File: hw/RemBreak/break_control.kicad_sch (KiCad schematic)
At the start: 13 parts, among them J6 Conn_01x07, J7 Conn_01x07, J8 Conn_01x03, Q10 BC337, Q11 BC847

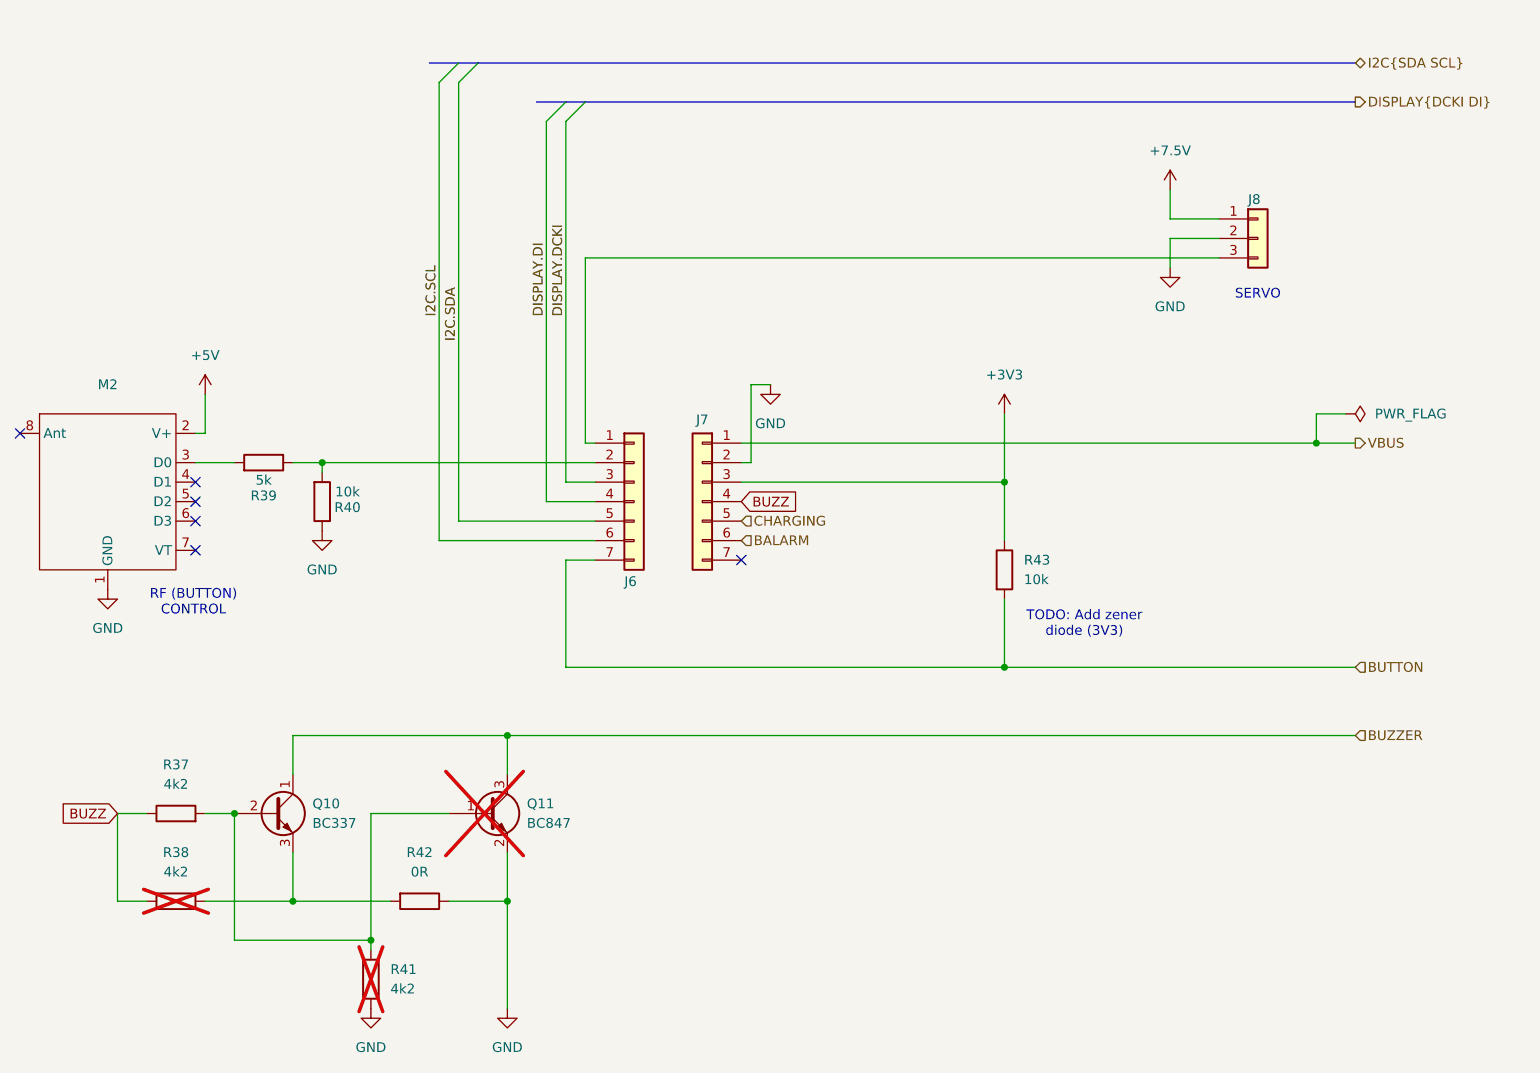
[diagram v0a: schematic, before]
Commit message: first version of routing finished
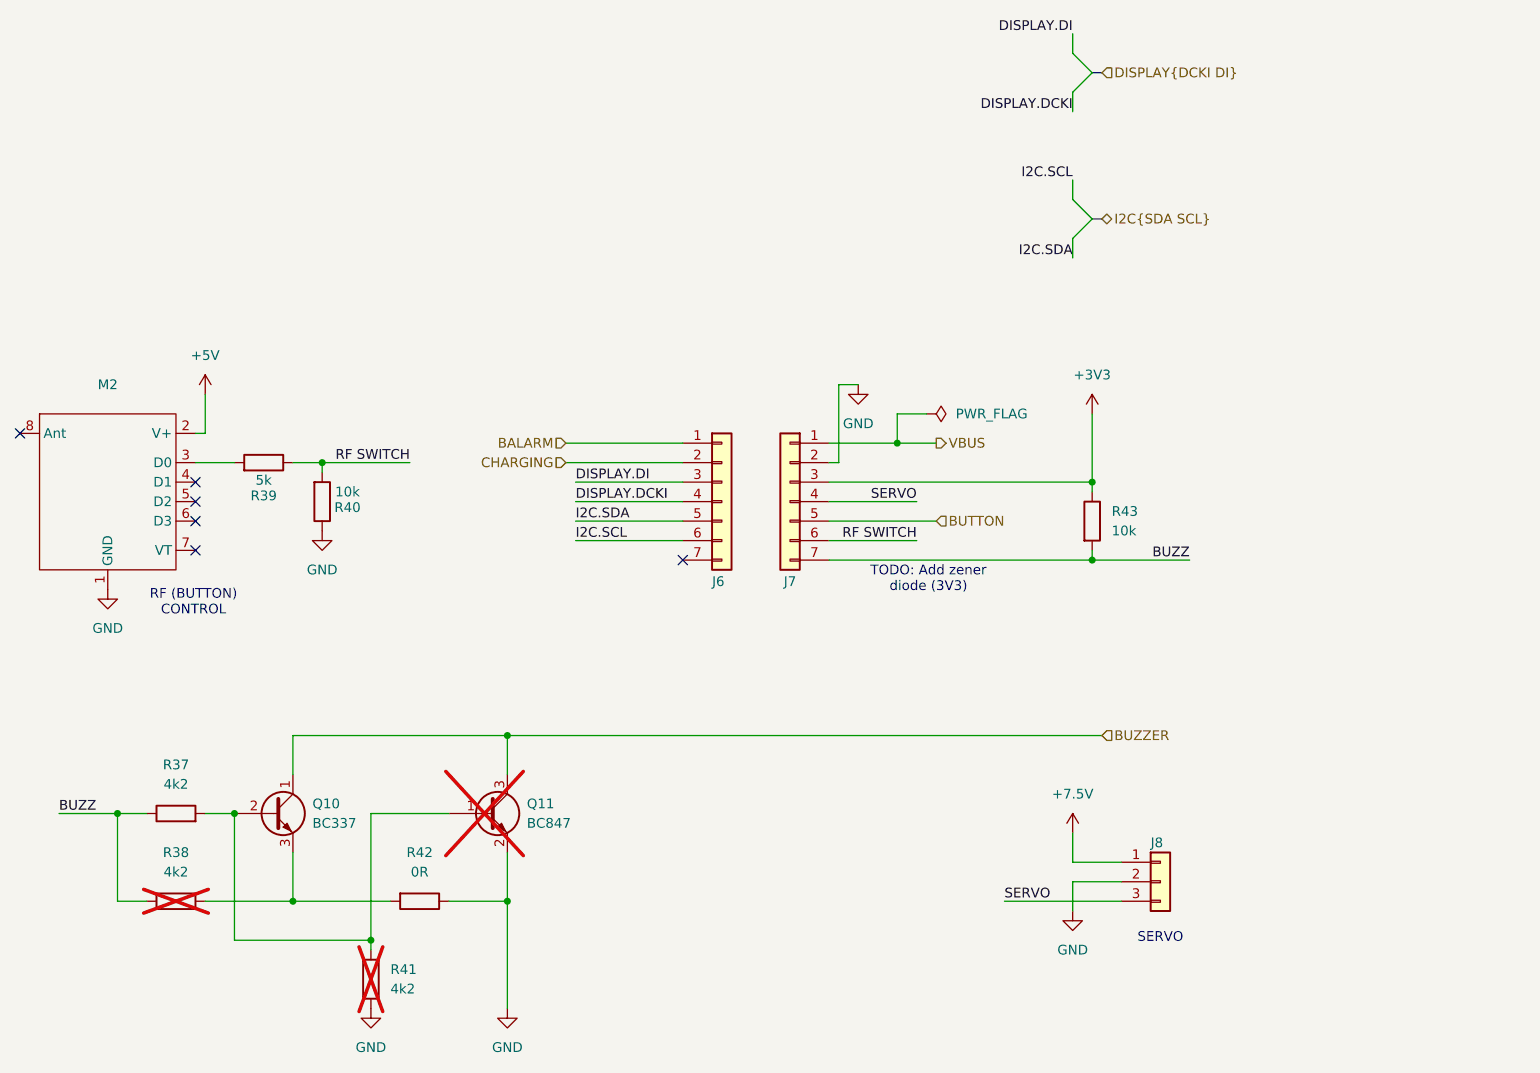
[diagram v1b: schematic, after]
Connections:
- net BALARM: now also J6.1 (Pin_1); no longer J7.6 (Pin_6)
- net BUTTON: now also J7.5 (Pin_5); no longer J6.7 (Pin_7), R43.2
- net BUZZ: now also J7.7 (Pin_7), R43.2; no longer J7.4 (Pin_4)
- net CHARGING: now also J6.2 (Pin_2); no longer J7.5 (Pin_5)
- net DISPLAY.DCKI: now also J6.4 (Pin_4); no longer J6.3 (Pin_3)
- net DISPLAY.DI: now also J6.3 (Pin_3); no longer J6.4 (Pin_4)
- net SERVO: now reaches J8.3 (Pin_3)
- net SERVO: now also J7.4 (Pin_4); no longer J6.1 (Pin_1)
- net RF SWITCH: now reaches R39.1, R40.2
- net RF SWITCH: now also J7.6 (Pin_6); no longer J6.2 (Pin_2)
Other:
- moved on the sheet: J6, J7, J8, R43

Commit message: changed board settings and replaced r and c footprints with the ones for handsoldering
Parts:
- R37, R38, R39, R40, R41, R42, R43: footprint Resistor_SMD:R_0805_2012Metric -> Resistor_SMD:R_0805_2012Metric_Pad1.20x1.40mm_HandSolder
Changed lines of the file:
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@@
 			)
 		)
-		(property "Footprint" "Resistor_SMD:R_0805_2012Metric"
+		(property "Footprint" "Resistor_SMD:R_0805_2012Metric_Pad1.20x1.40mm_HandSolder"
 			(at 74.93 136.398 90)
 			(effects
@@
 			)
 		)
-		(property "Footprint" "Resistor_SMD:R_0805_2012Metric"
+		(property "Footprint" "Resistor_SMD:R_0805_2012Metric_Pad1.20x1.40mm_HandSolder"
 			(at 192.532 96.52 90)
 			(effects
@@
 			)
 		)
-		(property "Footprint" "Resistor_SMD:R_0805_2012Metric"
+		(property "Footprint" "Resistor_SMD:R_0805_2012Metric_Pad1.20x1.40mm_HandSolder"
 			(at 106.68 144.272 90)
 			(effects
@@
 			)
 		)
-		(property "Footprint" "Resistor_SMD:R_0805_2012Metric"
+		(property "Footprint" "Resistor_SMD:R_0805_2012Metric_Pad1.20x1.40mm_HandSolder"
 			(at 74.93 147.828 90)
 			(effects
@@
 			)
 		)
-		(property "Footprint" "Resistor_SMD:R_0805_2012Metric"
+		(property "Footprint" "Resistor_SMD:R_0805_2012Metric_Pad1.20x1.40mm_HandSolder"
 			(at 102.108 156.21 90)
 			(effects
@@
 			)
 		)
-		(property "Footprint" "Resistor_SMD:R_0805_2012Metric"
+		(property "Footprint" "Resistor_SMD:R_0805_2012Metric_Pad1.20x1.40mm_HandSolder"
 			(at 86.36 90.678 90)
 			(effects
@@
 			)
 		)
-		(property "Footprint" "Resistor_SMD:R_0805_2012Metric"
+		(property "Footprint" "Resistor_SMD:R_0805_2012Metric_Pad1.20x1.40mm_HandSolder"
 			(at 92.202 93.98 90)
 			(effects

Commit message: components placed and tracks routed - missing gnd connections and have to refactor the resistors under MCU
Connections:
- net BUTTON: now also J7.6 (Pin_6); no longer J7.5 (Pin_5)
- net CHARGING: now also J7.5 (Pin_5); no longer J6.2 (Pin_2)
- net RF SWITCH: now also J6.2 (Pin_2); no longer J7.6 (Pin_6)
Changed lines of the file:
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@@
+	(wire
+		(pts
+			(xy 127 88.9) (xy 140.97 88.9)
+		)
+		(stroke
+			(width 0)
+			(type default)
+		)
+	)
 	(wire
 		(pts
@@
 	(wire
 		(pts
-			(xy 160.02 99.06) (xy 171.45 99.06)
-		)
-		(stroke
-			(width 0)
-			(type default)
-		)
-	)
-	(wire
-		(pts
-			(xy 125.73 88.9) (xy 140.97 88.9)
+			(xy 160.02 99.06) (xy 173.99 99.06)
 		)
 		(stroke
@@
 	)
 	(label "RF SWITCH"
-		(at 171.45 99.06 180)
-		(fields_autoplaced yes)
-		(effects
-			(font
-				(size 1.27 1.27)
-			)
-			(justify right bottom)
+		(at 127 88.9 0)
+		(fields_autoplaced yes)
+		(effects
+			(font
+				(size 1.27 1.27)
+			)
+			(justify left bottom)
 		)
 	)
@@
 	(hierarchical_label "BUTTON"
 		(shape input)
-		(at 173.99 96.52 0)
+		(at 173.99 99.06 0)
 		(fields_autoplaced yes)
 		(effects
@@
 	(hierarchical_label "CHARGING"
 		(shape input)
-		(at 125.73 88.9 180)
-		(fields_autoplaced yes)
-		(effects
-			(font
-				(size 1.27 1.27)
-			)
-			(justify right)
-		)
-	)
+		(at 173.99 96.52 0)
+		(fields_autoplaced yes)
+		(effects
+			(font
+				(size 1.27 1.27)
+			)
+			(justify left)
+		)
+	)

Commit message: adjusting layout
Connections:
- net BALARM: now also J6.2 (Pin_2); no longer J6.1 (Pin_1)
- net RF SWITCH: now also J6.1 (Pin_1); no longer J6.2 (Pin_2)
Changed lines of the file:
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@@
 	(wire
 		(pts
-			(xy 125.73 86.36) (xy 140.97 86.36)
+			(xy 125.73 88.9) (xy 140.97 88.9)
 		)
 		(stroke
@@
 	(wire
 		(pts
-			(xy 127 88.9) (xy 140.97 88.9)
+			(xy 127 86.36) (xy 140.97 86.36)
 		)
 		(stroke
@@
 	)
 	(label "RF SWITCH"
-		(at 127 88.9 0)
+		(at 127 86.36 0)
 		(fields_autoplaced yes)
 		(effects
@@
 	(hierarchical_label "BALARM"
 		(shape input)
-		(at 125.73 86.36 180)
-		(fields_autoplaced yes)
-		(effects
+		(at 125.73 88.9 180)
+		(fields_autoplaced yes)
+		(effects

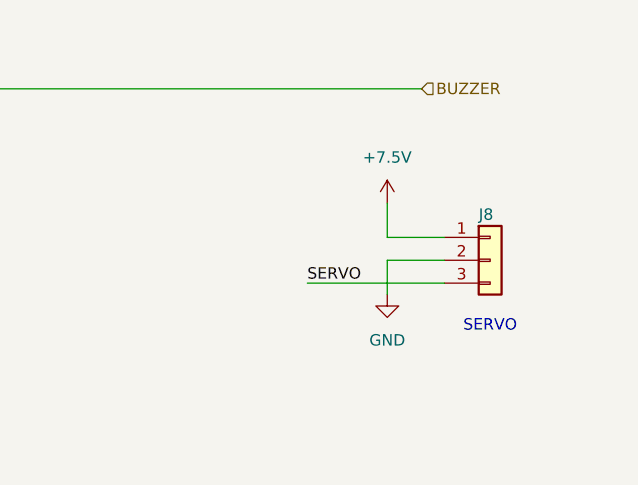
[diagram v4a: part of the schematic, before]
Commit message: middle part rerouted to fix the gnd connection
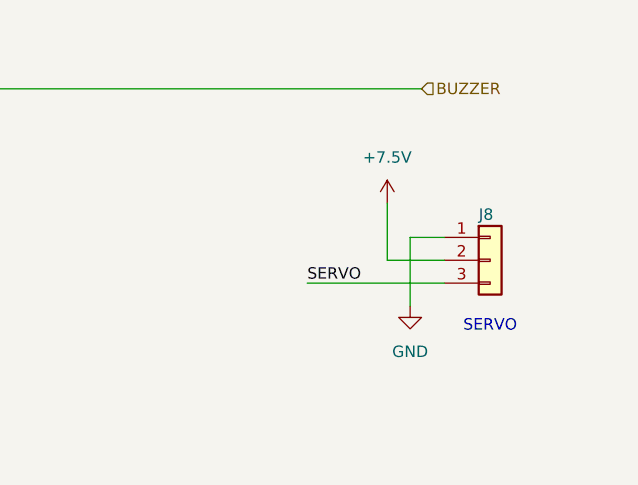
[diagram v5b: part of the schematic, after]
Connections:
- net +7.5V: now also J8.2 (Pin_2); no longer J8.1 (Pin_1)
- net GND: now also J8.1 (Pin_1); no longer J8.2 (Pin_2)
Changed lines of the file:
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@@
+	(wire
+		(pts
+			(xy 191.77 137.16) (xy 191.77 143.51)
+		)
+		(stroke
+			(width 0)
+			(type default)
+		)
+	)
 	(wire
 		(pts
@@
 	(wire
 		(pts
+			(xy 194.31 148.59) (xy 194.31 140.97)
+		)
+		(stroke
+			(width 0)
+			(type default)
+		)
+	)
+	(wire
+		(pts
 			(xy 182.88 146.05) (xy 198.12 146.05)
 		)
@@
 	(wire
 		(pts
+			(xy 191.77 143.51) (xy 198.12 143.51)
+		)
+		(stroke
+			(width 0)
+			(type default)
+		)
+	)
+	(wire
+		(pts
 			(xy 160.02 99.06) (xy 173.99 99.06)
 		)
@@
 	(wire
 		(pts
-			(xy 191.77 143.51) (xy 191.77 147.32)
-		)
-		(stroke
-			(width 0)
-			(type default)
-		)
-	)
-	(wire
-		(pts
 			(xy 100.33 134.62) (xy 110.49 134.62)
 		)
@@
 	(wire
 		(pts
-			(xy 191.77 140.97) (xy 198.12 140.97)
-		)
-		(stroke
-			(width 0)
-			(type default)
-		)
-	)
-	(wire
-		(pts
 			(xy 160.02 91.44) (xy 194.31 91.44)
 		)
@@
 		)
 	)
-	(wire
-		(pts
-			(xy 198.12 143.51) (xy 191.77 143.51)
-		)
-		(stroke
-			(width 0)
-			(type default)
-		)
-	)
 	(bus
 		(pts
@@
 	(wire
 		(pts
-			(xy 191.77 137.16) (xy 191.77 140.97)
-		)
-		(stroke
-			(width 0)
-			(type default)
-		)
-	)
-	(wire
-		(pts
 			(xy 160.02 86.36) (xy 168.91 86.36)
 		)
@@
 		(pts
 			(xy 191.77 33.02) (xy 191.77 35.56)
+		)
+		(stroke
+			(width 0)
+			(type default)
+		)
+	)
+	(wire
+		(pts
+			(xy 194.31 140.97) (xy 198.12 140.97)
 		)
 		(stroke
@@
 	(symbol
 		(lib_id "power:GND")
-		(at 191.77 147.32 0)
+		(at 194.31 148.59 0)
 		(unit 1)
 		(exclude_from_sim no)
@@
 		(fields_autoplaced yes)
 		(property "Reference" "#PWR044"
-			(at 191.77 153.67 0)
+			(at 194.31 154.94 0)
 			(effects
 				(font
@@
 		)
 		(property "Value" "GND"
-			(at 191.77 152.4 0)
+			(at 194.31 153.67 0)
 			(effects
 				(font
@@
 		)
 		(property "Footprint" ""
-			(at 191.77 147.32 0)
+			(at 194.31 148.59 0)
 			(effects
 				(font
@@
 		)
 		(property "Datasheet" ""
-			(at 191.77 147.32 0)
+			(at 194.31 148.59 0)
 			(effects
 				(font
@@
 		)
 		(property "Description" "Power symbol creates a global label with name \"GND\" , ground"
-			(at 191.77 147.32 0)
-			(effects
-				(font
+			(at 194.31 148.59 0)
+			(effects
+				(font

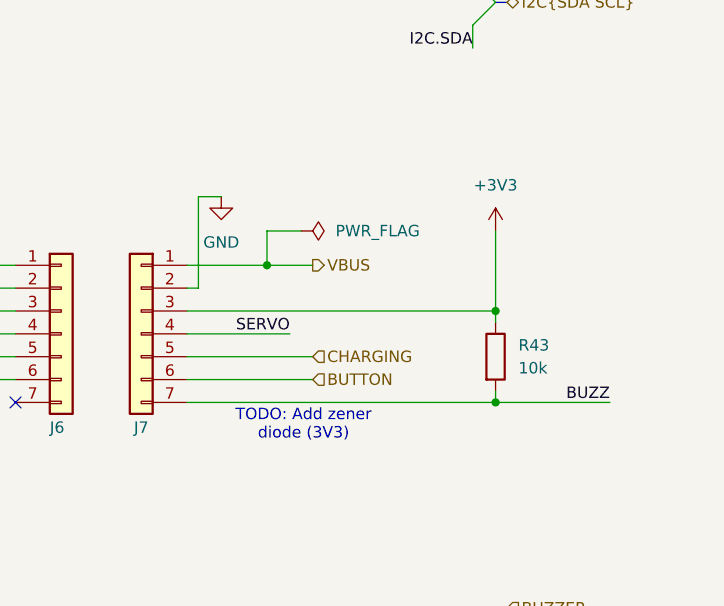
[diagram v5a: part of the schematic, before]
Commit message: finished routing - drc did not pass
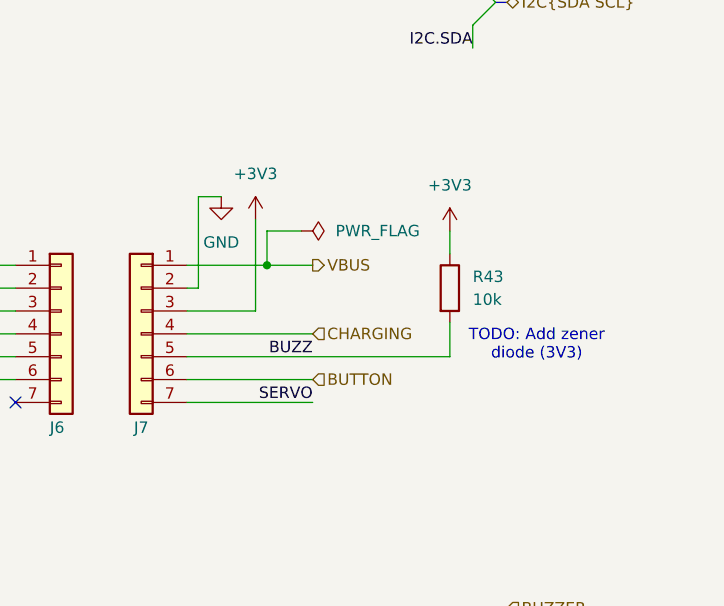
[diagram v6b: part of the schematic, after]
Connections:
- net BUZZ: now also J7.5 (Pin_5); no longer J7.7 (Pin_7)
- net CHARGING: now also J7.4 (Pin_4); no longer J7.5 (Pin_5)
- net SERVO: now also J7.7 (Pin_7); no longer J7.4 (Pin_4)
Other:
- moved on the sheet: R43
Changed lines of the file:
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@@
 	(text "TODO: Add zener \ndiode (3V3)"
 		(exclude_from_sim no)
-		(at 172.974 104.14 0)
+		(at 198.882 95.25 0)
 		(effects
 			(font
@@
 	)
 	(junction
-		(at 194.31 91.44)
-		(diameter 0)
-		(color 0 0 0 0)
-	)
-	(junction
 		(at 93.98 88.9)
 		(diameter 0)
@@
 	)
 	(junction
-		(at 194.31 101.6)
-		(diameter 0)
-		(color 0 0 0 0)
-	)
-	(junction
 		(at 90.17 146.05)
 		(diameter 0)
@@
 	(wire
 		(pts
+			(xy 160.02 101.6) (xy 173.99 101.6)
+		)
+		(stroke
+			(width 0)
+			(type default)
+		)
+	)
+	(wire
+		(pts
 			(xy 118.11 124.46) (xy 118.11 129.54)
 		)
@@
 	(wire
 		(pts
-			(xy 194.31 82.55) (xy 194.31 91.44)
-		)
-		(stroke
-			(width 0)
-			(type default)
-		)
-	)
-	(wire
-		(pts
 			(xy 191.77 54.61) (xy 191.77 52.07)
 		)
@@
 	(wire
 		(pts
-			(xy 194.31 91.44) (xy 194.31 92.71)
-		)
-		(stroke
-			(width 0)
-			(type default)
-		)
-	)
-	(wire
-		(pts
 			(xy 127 99.06) (xy 140.97 99.06)
 		)
@@
 	(wire
 		(pts
+			(xy 167.64 81.28) (xy 167.64 91.44)
+		)
+		(stroke
+			(width 0)
+			(type default)
+		)
+	)
+	(wire
+		(pts
 			(xy 59.69 134.62) (xy 67.31 134.62)
 		)
@@
 	(wire
 		(pts
-			(xy 160.02 101.6) (xy 194.31 101.6)
-		)
-		(stroke
-			(width 0)
-			(type default)
-		)
-	)
-	(wire
-		(pts
 			(xy 191.77 143.51) (xy 198.12 143.51)
 		)
@@
 	(wire
 		(pts
+			(xy 160.02 93.98) (xy 173.99 93.98)
+		)
+		(stroke
+			(width 0)
+			(type default)
+		)
+	)
+	(wire
+		(pts
 			(xy 160.02 99.06) (xy 173.99 99.06)
 		)
@@
 	(wire
 		(pts
-			(xy 194.31 101.6) (xy 207.01 101.6)
-		)
-		(stroke
-			(width 0)
-			(type default)
-		)
-	)
-	(wire
-		(pts
-			(xy 160.02 96.52) (xy 173.99 96.52)
-		)
-		(stroke
-			(width 0)
-			(type default)
-		)
-	)
-	(wire
-		(pts
 			(xy 100.33 134.62) (xy 110.49 134.62)
 		)
@@
 	(wire
 		(pts
+			(xy 167.64 91.44) (xy 160.02 91.44)
+		)
+		(stroke
+			(width 0)
+			(type default)
+		)
+	)
+	(wire
+		(pts
 			(xy 168.91 82.55) (xy 168.91 86.36)
 		)
@@
 		)
 	)
-	(wire
-		(pts
-			(xy 160.02 91.44) (xy 194.31 91.44)
-		)
-		(stroke
-			(width 0)
-			(type default)
-		)
-	)
 	(bus
 		(pts
@@
 	(wire
 		(pts
-			(xy 194.31 100.33) (xy 194.31 101.6)
-		)
-		(stroke
-			(width 0)
-			(type default)
-		)
-	)
-	(wire
-		(pts
 			(xy 78.74 85.09) (xy 77.47 85.09)
 		)
@@
 	(wire
 		(pts
-			(xy 160.02 93.98) (xy 171.45 93.98)
+			(xy 160.02 96.52) (xy 189.23 96.52)
 		)
 		(stroke
@@
 		(pts
 			(xy 127 96.52) (xy 140.97 96.52)
+		)
+		(stroke
+			(width 0)
+			(type default)
+		)
+	)
+	(wire
+		(pts
+			(xy 189.23 82.55) (xy 189.23 85.09)
+		)
+		(stroke
+			(width 0)
+			(type default)
+		)
+	)
+	(wire
+		(pts
+			(xy 189.23 92.71) (xy 189.23 96.52)
 		)
 		(stroke
@@
 	)
 	(label "SERVO"
-		(at 171.45 93.98 180)
+		(at 173.99 101.6 180)
 		(fields_autoplaced yes)
 		(effects
@@
 	)
 	(label "BUZZ"
-		(at 207.01 101.6 180)
+		(at 173.99 96.52 180)
 		(fields_autoplaced yes)
 		(effects
@@
 	(hierarchical_label "CHARGING"
 		(shape input)
-		(at 173.99 96.52 0)
+		(at 173.99 93.98 0)
 		(fields_autoplaced yes)
 		(effects
@@
 	(symbol
 		(lib_id "Device:R")
-		(at 194.31 96.52 0)
+		(at 189.23 88.9 0)
 		(unit 1)
 		(exclude_from_sim no)
@@
 		(fields_autoplaced yes)
 		(property "Reference" "R43"
-			(at 196.85 95.2499 0)
+			(at 191.77 87.6299 0)
 			(effects
 				(font
@@
 		)
 		(property "Value" "10k"
-			(at 196.85 97.7899 0)
+			(at 191.77 90.1699 0)
 			(effects
 				(font
@@
 		)
 		(property "Footprint" "Resistor_SMD:R_0805_2012Metric_Pad1.20x1.40mm_HandSolder"
-			(at 192.532 96.52 90)
+			(at 187.452 88.9 90)
 			(effects
 				(font
@@
 		)
 		(property "Datasheet" "~"
-			(at 194.31 96.52 0)
+			(at 189.23 88.9 0)
 			(effects
 				(font
@@
 		)
 		(property "Description" "Resistor"
-			(at 194.31 96.52 0)
+			(at 189.23 88.9 0)
 			(effects
 				(font
@@
 	(symbol
 		(lib_id "power:+3V3")
-		(at 194.31 82.55 0)
+		(at 167.64 81.28 0)
 		(unit 1)
 		(exclude_from_sim no)
@@
 		(fields_autoplaced yes)
 		(property "Reference" "#PWR042"
-			(at 194.31 86.36 0)
+			(at 167.64 85.09 0)
 			(effects
 				(font
@@
 		)
 		(property "Value" "+3V3"
-			(at 194.31 77.47 0)
+			(at 167.64 76.2 0)
 			(effects
 				(font
@@
 		)
 		(property "Footprint" ""
-			(at 194.31 82.55 0)
+			(at 167.64 81.28 0)
 			(effects
 				(font
@@
 		)
 		(property "Datasheet" ""
-			(at 194.31 82.55 0)
+			(at 167.64 81.28 0)
 			(effects
 				(font
@@
 		)
 		(property "Description" "Power symbol creates a global label with name \"+3V3\""
-			(at 194.31 82.55 0)
+			(at 167.64 81.28 0)
 			(effects
 				(font
@@
 					(unit 1)
 				)
+			)
+		)
+	)
+	(symbol
+		(lib_id "power:+3V3")
+		(at 189.23 82.55 0)
+		(unit 1)
+		(exclude_from_sim no)
+		(in_bom yes)
+		(on_board yes)
+		(dnp no)
+		(fields_autoplaced yes)
+		(property "Reference" "#PWR045"
+			(at 189.23 86.36 0)
+			(effects
+				(font
+					(size 1.27 1.27)
+				)
+				(hide yes)
+			)
+		)
+		(property "Value" "+3V3"
+			(at 189.23 77.47 0)
+			(effects
+				(font
+					(size 1.27 1.27)
+				)
+			)
+		)
+		(property "Footprint" ""
+			(at 189.23 82.55 0)
+			(effects
+				(font
+					(size 1.27 1.27)
+				)
+				(hide yes)
+			)
+		)
+		(property "Datasheet" ""
+			(at 189.23 82.55 0)
+			(effects
+				(font
+					(size 1.27 1.27)
+				)
+				(hide yes)
+			)
+		)
+		(property "Description" "Power symbol creates a global label with name \"+3V3\""
+			(at 189.23 82.55 0)
+			(effects
+				(font
+					(size 1.27 1.27)
+				)
+				(hide yes)
+			)
+		)
+		(pin "1"
+		)
+		(instances
+			(project "RemBreak"
+				(path "/e6d4ae5b-c9d7-4cbe-b288-c929fdf55a75/4813b76c-f465-42f9-8515-5ce5d55b4403"
+					(reference "#PWR045")
+					(unit 1)
+				)
